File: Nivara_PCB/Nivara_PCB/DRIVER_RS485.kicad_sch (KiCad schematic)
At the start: 7 parts, among them U5 RSM3485ECHT_C2992406

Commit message: TERMINACIONES Y AJUSTES FINALES
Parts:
- removed C9: 10uF, PCM_Capacitor_SMD_AKL:C_0603_1608Metric, symbol EasyEDA:C_0603
- removed R7: R_0603, PCM_Resistor_SMD_AKL:R_0603_1608Metric, symbol EasyEDA:R_0603
- added C9: 10uF, Capacitor_SMD:CP_Elec_4x5.4, symbol Device:C_Polarized
- added JP2, JP3: SolderJumper_2_Open, Jumper:SolderJumper-2_P1.3mm_Open_Pad1.0x1.5mm, symbol EasyEDA:SolderJumper_2_Open
- D7: renamed from D6; LCSC Part (none) -> C87074; Part # (none) -> SMAJ5.0A-13-F
- D8: LCSC Part (none) -> C83267; Part # (none) -> SMAJ12CA-13-F
- D9: renamed from D7; LCSC Part (none) -> C32677; Part # (none) -> PSM712-LF-T7
- R12: renamed from R8; value R_0603 -> 120; LCSC Part (none) -> C22787; Part # (none) -> 0603WAF1200T5E
- U7: renamed from U5; Part # (none) -> RSM3485ECHT
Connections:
- net +3.3V: now also C9.1
- net GND: now also C9.2
- net RS485_A+: now also D8.1 (K), D9.1 (A1), U7.9 (A), JP3.2 (B)
- net RS485_B-: now also D8.2 (A), D9.2 (A2), U7.8 (B), JP2.2 (B); no longer R12.2
- new net: JP2.1 (A), R12.1
- new net: JP3.1 (A), R12.2
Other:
- moved on the sheet: R12

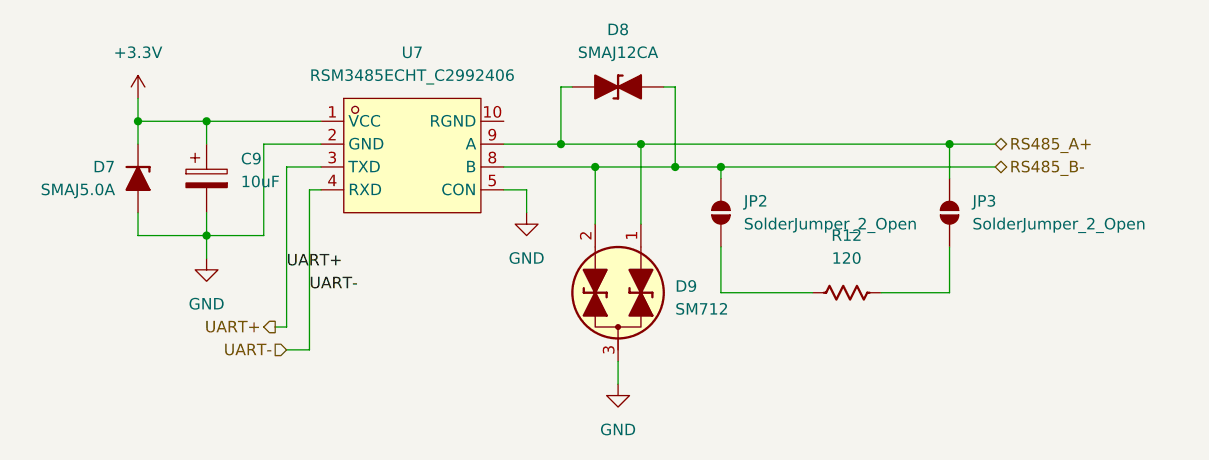
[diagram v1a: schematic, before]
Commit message: Cambios en las silscreen de los componentes.
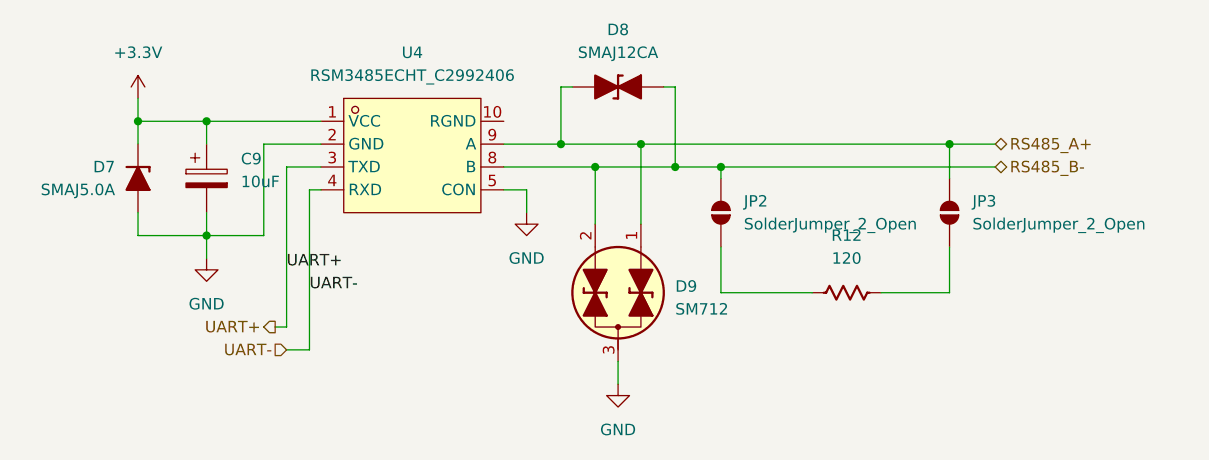
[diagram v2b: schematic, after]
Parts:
- renumbered U7 to U4
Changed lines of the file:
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@@
 		(dnp no)
 		(fields_autoplaced yes)
-		(property "Reference" "#PWR029"
+		(property "Reference" "#PWR031"
 			(at 130.81 97.79 0)
 			(effects
@@
 			(project "Nivara_PCB"
 				(path "/13184db0-a71d-4054-b13a-bbf46d2b100d/4e7fa7f2-8bf5-4f9c-874d-fa1b4fd76f92/3eeaffcc-9bb5-4f36-a3b6-9bf8c04eaeb0"
-					(reference "#PWR029")
+					(reference "#PWR031")
 					(unit 1)
 				)
@@
 		(dnp no)
 		(fields_autoplaced yes)
-		(property "Reference" "#PWR027"
+		(property "Reference" "#PWR029"
 			(at 85.09 83.82 0)
 			(effects
@@
 			(project "Nivara_PCB"
 				(path "/13184db0-a71d-4054-b13a-bbf46d2b100d/4e7fa7f2-8bf5-4f9c-874d-fa1b4fd76f92/3eeaffcc-9bb5-4f36-a3b6-9bf8c04eaeb0"
-					(reference "#PWR027")
+					(reference "#PWR029")
 					(unit 1)
 				)
@@
 		(dnp no)
 		(fields_autoplaced yes)
-		(property "Reference" "U7"
+		(property "Reference" "U4"
 			(at 107.95 54.61 0)
 			(effects
@@
 			(project ""
 				(path "/13184db0-a71d-4054-b13a-bbf46d2b100d/4e7fa7f2-8bf5-4f9c-874d-fa1b4fd76f92/3eeaffcc-9bb5-4f36-a3b6-9bf8c04eaeb0"
-					(reference "U7")
+					(reference "U4")
 					(unit 1)
 				)
@@
 		(dnp no)
 		(fields_autoplaced yes)
-		(property "Reference" "#PWR026"
+		(property "Reference" "#PWR028"
 			(at 77.47 63.5 0)
 			(effects
@@
 			(project "Nivara_PCB"
 				(path "/13184db0-a71d-4054-b13a-bbf46d2b100d/4e7fa7f2-8bf5-4f9c-874d-fa1b4fd76f92/3eeaffcc-9bb5-4f36-a3b6-9bf8c04eaeb0"
-					(reference "#PWR026")
+					(reference "#PWR028")
 					(unit 1)
 				)
@@
 		(dnp no)
 		(fields_autoplaced yes)
-		(property "Reference" "#PWR028"
+		(property "Reference" "#PWR030"
 			(at 120.65 78.74 0)
 			(effects
@@
 			(project "Nivara_PCB"
 				(path "/13184db0-a71d-4054-b13a-bbf46d2b100d/4e7fa7f2-8bf5-4f9c-874d-fa1b4fd76f92/3eeaffcc-9bb5-4f36-a3b6-9bf8c04eaeb0"
-					(reference "#PWR028")
-					(unit 1)
-				)
+					(reference "#PWR030")
+					(unit 1)
+				)

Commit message: Ya está la pcb hecha y el pedido de los componentes realizado, falta soldar y probar.
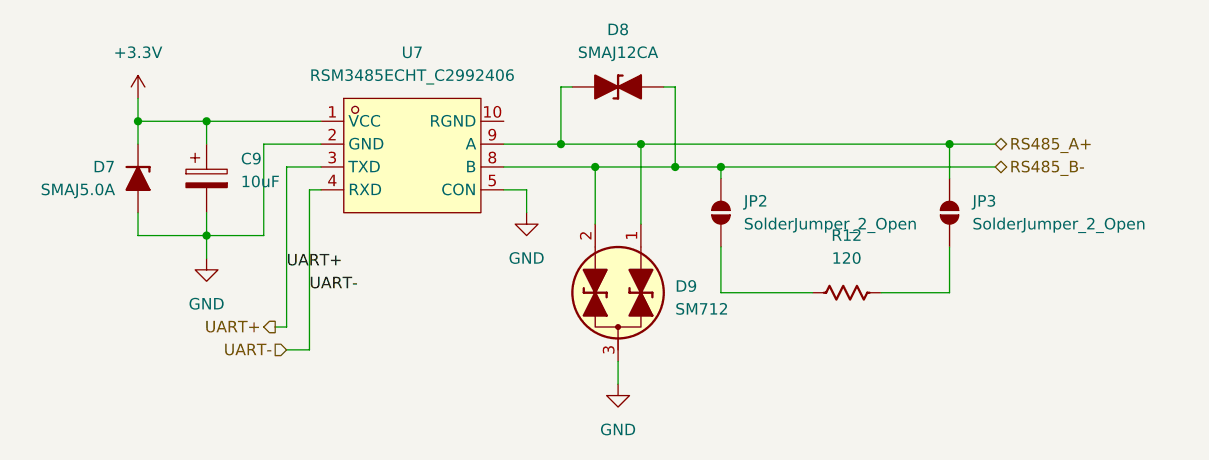
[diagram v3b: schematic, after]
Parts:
- renumbered U4 to U7
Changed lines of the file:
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@@
 		(dnp no)
 		(fields_autoplaced yes)
-		(property "Reference" "U4"
+		(property "Reference" "U7"
 			(at 107.95 54.61 0)
 			(effects
@@
 			(project ""
 				(path "/13184db0-a71d-4054-b13a-bbf46d2b100d/4e7fa7f2-8bf5-4f9c-874d-fa1b4fd76f92/3eeaffcc-9bb5-4f36-a3b6-9bf8c04eaeb0"
-					(reference "U4")
+					(reference "U7")
 					(unit 1)
 				)
